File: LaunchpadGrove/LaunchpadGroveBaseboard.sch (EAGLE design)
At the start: 13 parts

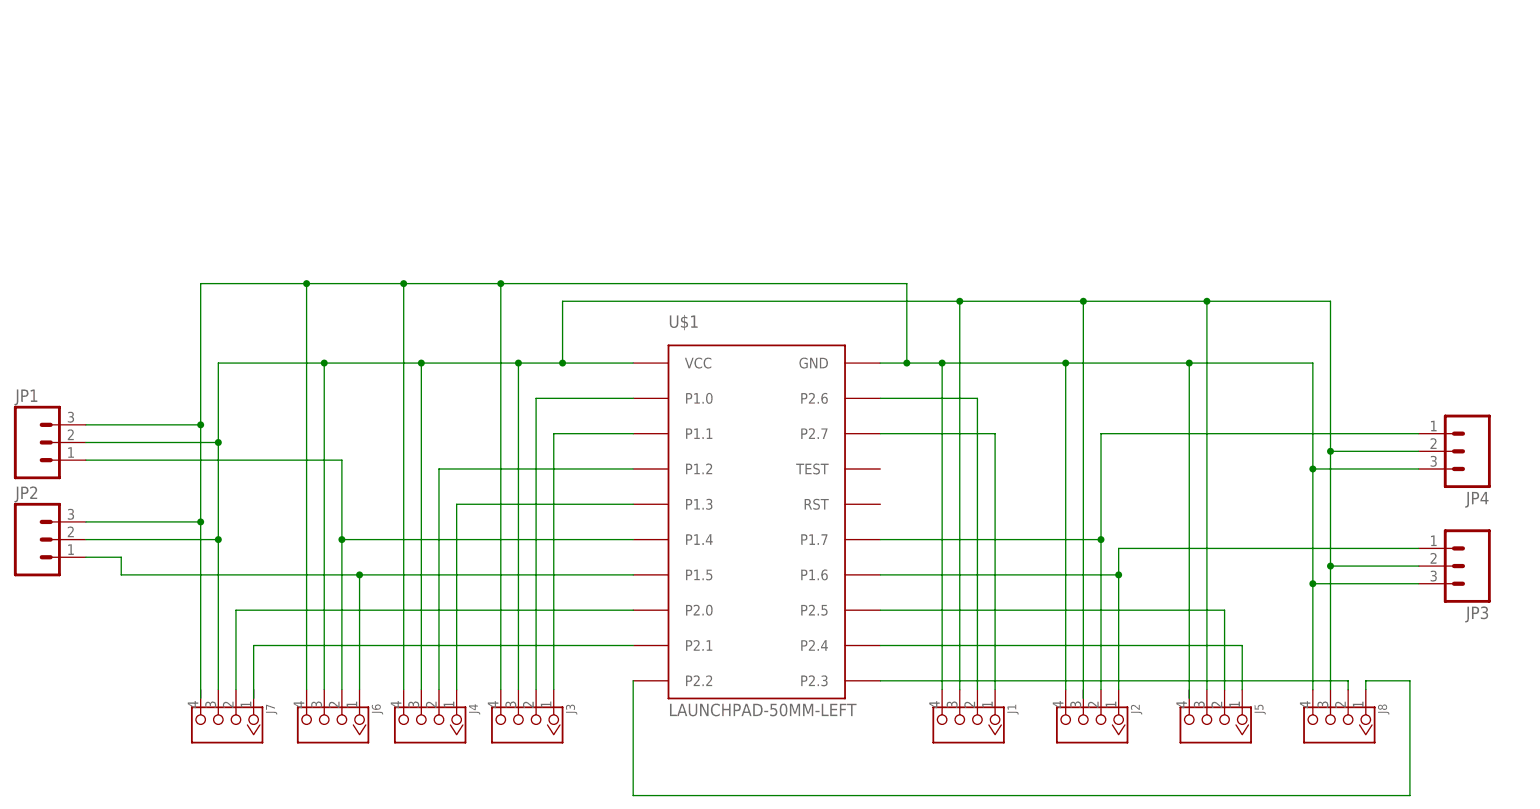
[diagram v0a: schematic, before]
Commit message: Added switch, vbat, cct protection etc
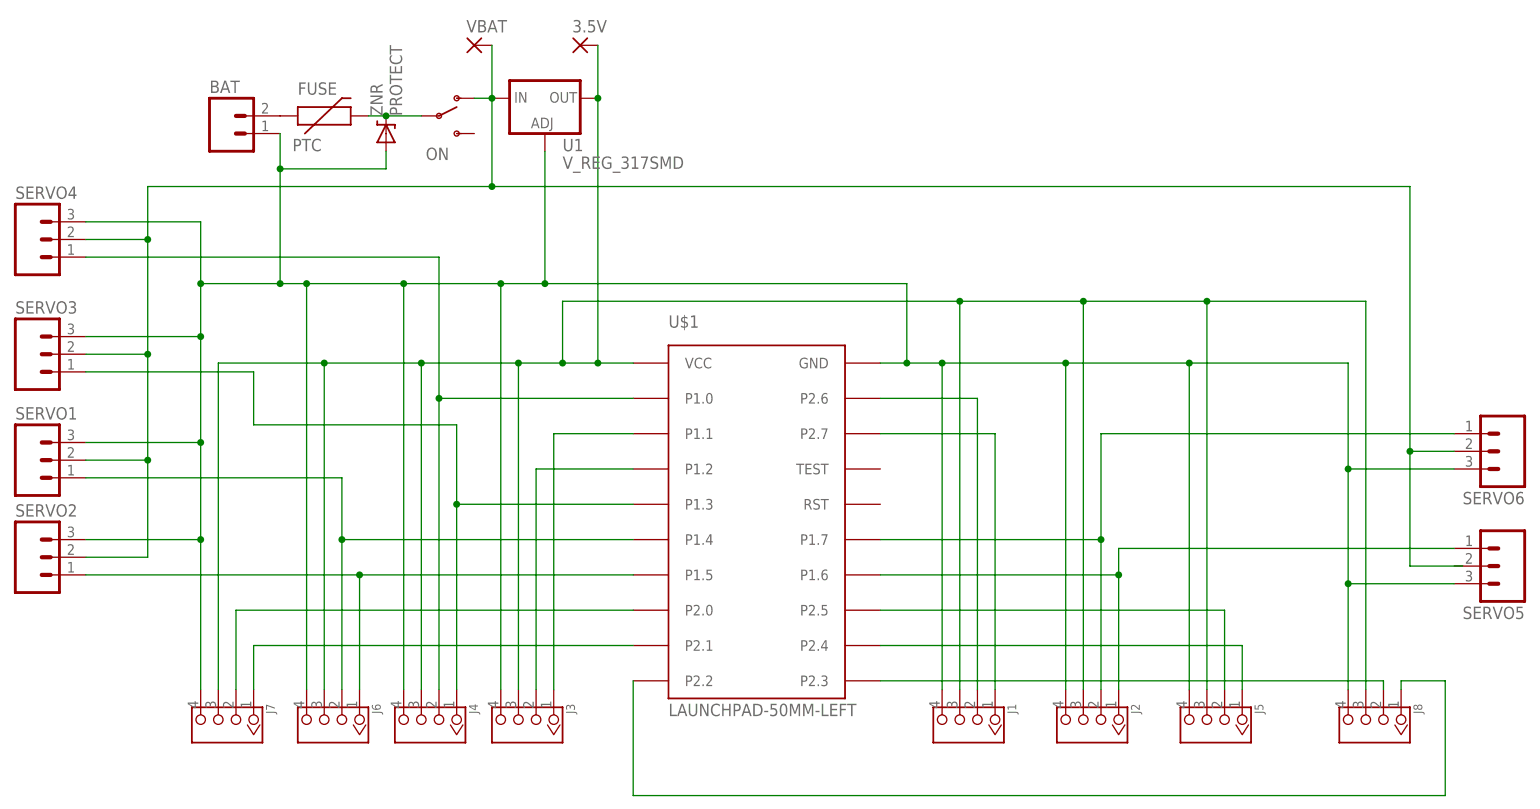
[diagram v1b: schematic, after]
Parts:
- removed JP1, JP2, JP3, JP4: (no value), SparkFun:M03PTH
- added 3.5V, VBAT: (no value), wirepad:2,15/1,0
- added BAT: (no value), SparkFun:M02PTH3
- added FUSE: PTC, SparkFun:PTCPTH
- added ON: (no value), SparkFun:SWITCH-SPSTPTH
- added SERVO1, SERVO2, SERVO3, SERVO4, SERVO5, SERVO6: (no value), SparkFun:M03PTH
- added U1: V_REG_317SMD, SparkFun:V_REG_317SMD
- added ZNR: PROTECT, SparkFun:DIODE-ZENERPTH
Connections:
- removed net N$5: J4.2, U$1.P1.2
- new net N$1: J3.2, U$1.P1.2
- new net N$16: FUSE.2, ON.P, ZNR.C
- new net N$2: BAT.2, FUSE.1
- new net VBAT: ON.O, SERVO1.2, SERVO2.2, SERVO3.2, SERVO4.2, SERVO6.2, U1.IN, VBAT.P
- net GND: now also BAT.1, J5.4, J7.4, SERVO1.3, SERVO2.3, SERVO3.3, SERVO4.3, SERVO5.3, SERVO6.3, U1.ADJ, ZNR.A; no longer JP1.3, JP2.3, JP3.3, JP4.3
- net N$11: now also SERVO6.1; no longer JP4.1
- net N$12: now also SERVO5.1; no longer JP3.1
- net N$3: now also J4.2, SERVO4.1; no longer J3.2
- net N$6: now also SERVO3.1
- net N$7: now also SERVO1.1; no longer JP1.1
- net N$8: now also SERVO2.1; no longer JP2.1
- net VCC: now also 3.5V.P, J2.3, U1.OUT; no longer JP1.2, JP2.2, JP3.2, JP4.2
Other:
- moved on the sheet: J8

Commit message: Space for larger zener
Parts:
- BAT: device SparkFun:M02PTH3 -> SparkFun:M02PTH
- ZNR: device SparkFun:DIODE-ZENERPTH -> diode:1N4004
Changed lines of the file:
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@@
 <part name="SERVO4" library="SparkFun" deviceset="M03" device="PTH"/>
 <part name="U1" library="SparkFun" deviceset="V_REG_317" device="SMD"/>
-<part name="BAT" library="SparkFun" deviceset="M02" device="PTH3"/>
+<part name="BAT" library="SparkFun" deviceset="M02" device="PTH"/>
 <part name="ON" library="SparkFun" deviceset="SWITCH-SPST" device="PTH"/>
-<part name="ZNR" library="SparkFun" deviceset="DIODE-ZENER" device="PTH" value="PROTECT"/>
+<part name="ZNR" library="diode" deviceset="1N4004" device="" value="PROTECT"/>
 <part name="VBAT" library="wirepad" deviceset="2,15/1,0" device=""/>
 <part name="3.5V" library="wirepad" deviceset="2,15/1,0" device=""/>
@@
 <instance part="BAT" gate="G$1" x="-119.38" y="121.92"/>
 <instance part="ON" gate="1" x="-88.9" y="124.46"/>
-<instance part="ZNR" gate="G$1" x="-96.52" y="121.92" smashed="yes" rot="R90">
+<instance part="ZNR" gate="1" x="-96.52" y="121.92" smashed="yes" rot="R90">
 <attribute name="NAME" x="-97.0026" y="124.46" size="1.778" layer="95" rot="R90"/>
 <attribute name="VALUE" x="-94.2086" y="124.46" size="1.778" layer="96" rot="R90"/>
@@
 <wire x1="-111.76" y1="121.92" x2="-111.76" y2="116.84" width="0.1524" layer="91"/>
 <junction x="-111.76" y="100.33"/>
-<pinref part="ZNR" gate="G$1" pin="A"/>
+<pinref part="ZNR" gate="1" pin="A"/>
 <wire x1="-111.76" y1="116.84" x2="-111.76" y2="100.33" width="0.1524" layer="91"/>
 <wire x1="-96.52" y1="119.38" x2="-96.52" y2="116.84" width="0.1524" layer="91"/>
@@
 <pinref part="ON" gate="1" pin="P"/>
 <wire x1="-99.06" y1="124.46" x2="-96.52" y2="124.46" width="0.1524" layer="91"/>
-<pinref part="ZNR" gate="G$1" pin="C"/>
+<pinref part="ZNR" gate="1" pin="C"/>
 <junction x="-96.52" y="124.46"/>
 <wire x1="-96.52" y1="124.46" x2="-91.44" y2="124.46" width="0.1524" layer="91"/>
